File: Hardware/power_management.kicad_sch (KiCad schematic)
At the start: 34 parts, among them J2 Conn_01x03, SW27 SW_DPDT_x2, U2 BQ24040, U3 BQ51050BRHL, U4 AP22814BW5

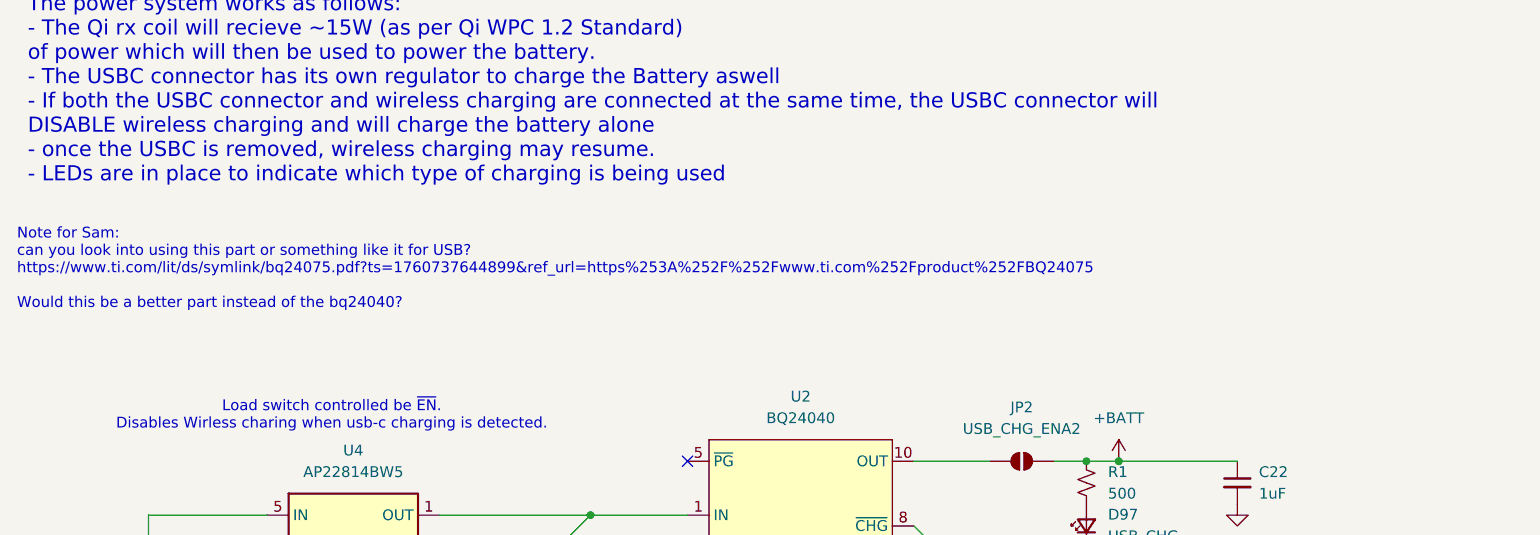
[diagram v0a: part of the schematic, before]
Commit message: Route dual sided hotswap/diodes assmebly
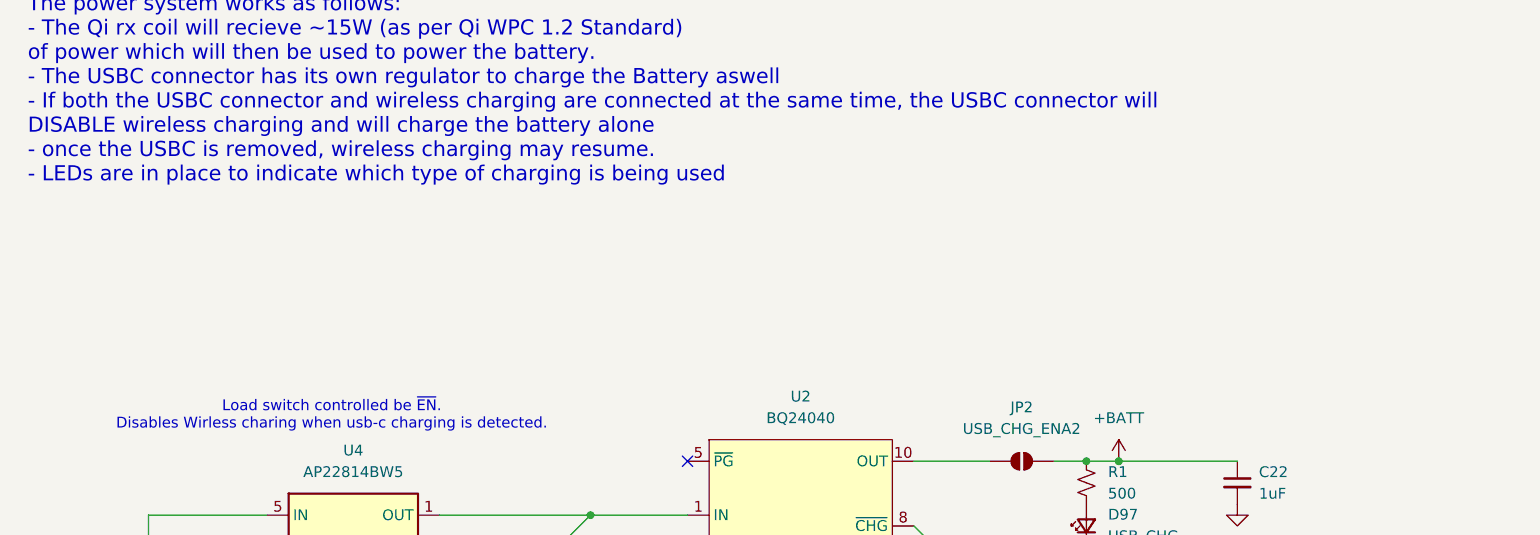
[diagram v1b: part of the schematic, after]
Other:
- note removed: "Note for Sam: can you look into using this part or something like it for USB? https://www.ti.com/lit/ds/symlink/bq24075.pdf?ts=1760737644899&ref_url=https%253A%252F%252Fwww.ti.com%252Fproduct%252FBQ24075 Would this be a better part instead of the bq24040?"
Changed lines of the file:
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@@
-		)
-	)
-	(text "Note for Sam:\ncan you look into using this part or something like it for USB?\nhttps://www.ti.com/lit/ds/symlink/bq24075.pdf?ts=1760737644899&ref_url=https%253A%252F%252Fwww.ti.com%252Fproduct%252FBQ24075\n\nWould this be a better part instead of the bq24040? "
-		(exclude_from_sim no)
-		(at 13.716 47.244 0)
-		(effects
-			(font
-				(size 1.27 1.27)
-			)
-			(justify left)
 		)
 	)

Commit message: added extra decoupling caps to the mcu VDD pins
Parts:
- J2: footprint Connector_JST:JST_GH_SM02B-GHS-TB_1x02-1MP_P1.25mm_Horizontal -> Connector_JST:JST_GH_SM03B-GHS-TB_1x03-1MP_P1.25mm_Horizontal
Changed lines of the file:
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@@
 			)
 		)
-		(property "Footprint" "Connector_JST:JST_GH_SM02B-GHS-TB_1x02-1MP_P1.25mm_Horizontal"
+		(property "Footprint" "Connector_JST:JST_GH_SM03B-GHS-TB_1x03-1MP_P1.25mm_Horizontal"
 			(at 190.5 128.27 0)
 			(effects

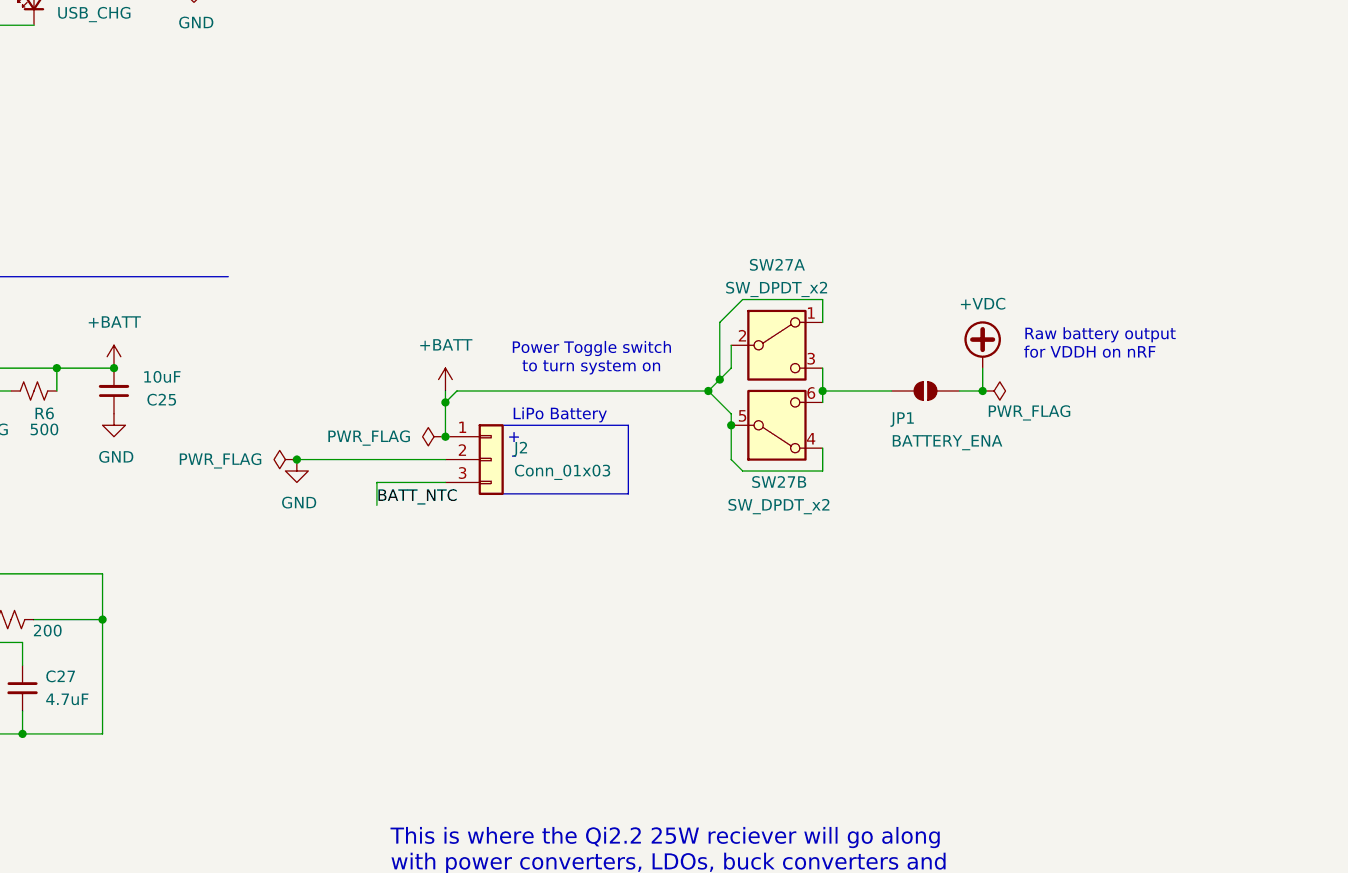
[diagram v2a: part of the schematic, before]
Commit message: added in pwoer mux
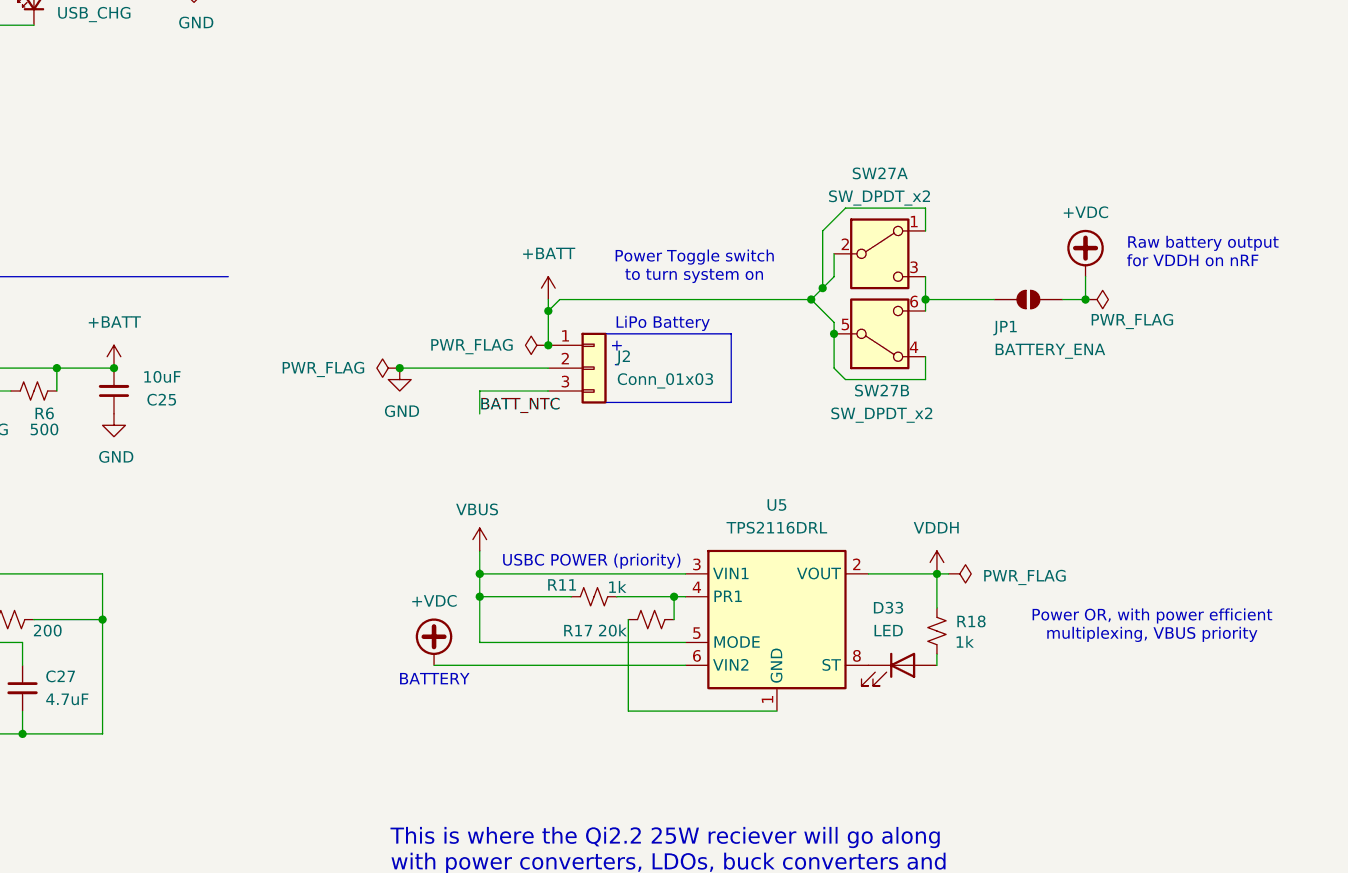
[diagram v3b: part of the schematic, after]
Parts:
- added D33: LED, symbol Device:LED
- added R11, R18: 1k, Resistor_SMD:R_0603_1608Metric, symbol Device:R_Small_US
- added R17: 20k, Resistor_SMD:R_0603_1608Metric, symbol Device:R_Small_US
- added U5: TPS2116DRL, Package_TO_SOT_SMD:SOT-583-8, symbol Power_Management:TPS2116DRL
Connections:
- net +VDC: now also U5.6 (VIN2)
- net VBUS: now also R11.1, U5.3 (VIN1), U5.5 (MODE)
- new net: R11.2, R17.1, U5.4 (PR1)
- new net: R17.2, U5.1 (GND)
- new net: D33.1 (K), U5.8 (ST)
- new net: D33.2 (A), R18.1
- new net VDDH: R18.2, U5.2 (VOUT), U5.7 (VOUT)
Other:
- note added: "BATTERY"
- note added: "Power OR, with power efficient multiplexing, VBUS priority"
- note added: "USBC POWER (priority)"
- moved on the sheet: J2, JP1, SW27A, SW27B

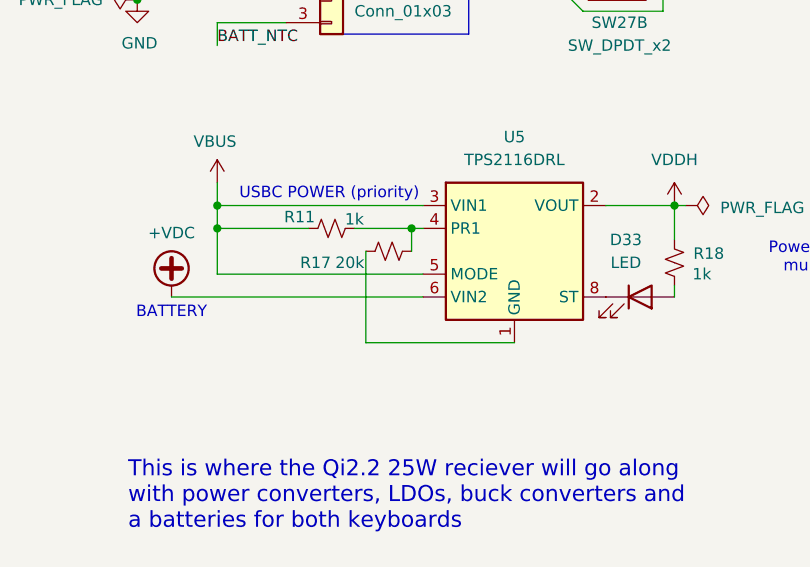
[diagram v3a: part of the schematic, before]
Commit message: modified layout placement
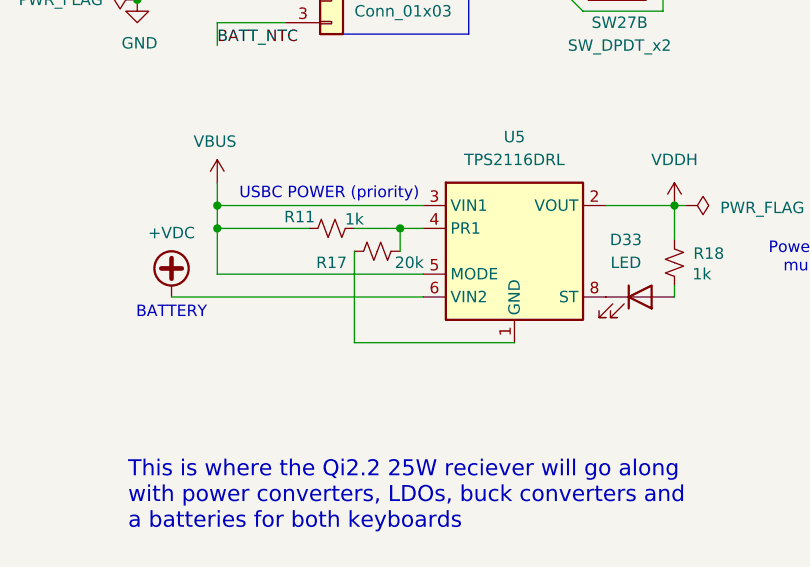
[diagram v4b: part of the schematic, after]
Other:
- moved on the sheet: R17
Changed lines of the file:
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@@
 	)
 	(junction
+		(at 209.55 143.51)
+		(diameter 0)
+		(color 0 0 0 0)
+	)
+	(junction
 		(at 227.33 109.22)
 		(diameter 0)
@@
 	)
 	(junction
-		(at 210.82 143.51)
-		(diameter 0)
-		(color 0 0 0 0)
-	)
-	(junction
 		(at 130.81 146.05)
 		(diameter 0)
@@
 		)
 	)
+	(wire
+		(pts
+			(xy 209.55 143.51) (xy 212.09 143.51)
+		)
+		(stroke
+			(width 0)
+			(type default)
+		)
+	)
 	(polyline
 		(pts
@@
 	(wire
 		(pts
-			(xy 205.74 146.05) (xy 205.74 156.21)
+			(xy 204.47 146.05) (xy 204.47 156.21)
 		)
 		(stroke
@@
 	(wire
 		(pts
-			(xy 210.82 143.51) (xy 212.09 143.51)
-		)
-		(stroke
-			(width 0)
-			(type default)
-		)
-	)
-	(wire
-		(pts
 			(xy 227.33 109.22) (xy 226.06 110.49)
 		)
@@
 	(wire
 		(pts
-			(xy 210.82 143.51) (xy 210.82 146.05)
+			(xy 209.55 143.51) (xy 209.55 146.05)
 		)
 		(stroke
@@
 	(wire
 		(pts
-			(xy 205.74 156.21) (xy 222.25 156.21)
+			(xy 204.47 156.21) (xy 222.25 156.21)
 		)
 		(stroke
@@
 	(wire
 		(pts
-			(xy 204.47 143.51) (xy 210.82 143.51)
+			(xy 204.47 143.51) (xy 209.55 143.51)
 		)
 		(stroke
@@
 	(symbol
 		(lib_id "Device:R_Small_US")
-		(at 208.28 146.05 270)
+		(at 207.01 146.05 270)
 		(unit 1)
 		(exclude_from_sim no)
@@
 		(dnp no)
 		(property "Reference" "R17"
-			(at 200.152 147.32 90)
+			(at 201.93 147.32 90)
 			(effects
 				(font
@@
 		)
 		(property "Value" "20k"
-			(at 203.962 147.32 90)
+			(at 210.566 147.32 90)
 			(effects
 				(font
@@
 		)
 		(property "Footprint" "Resistor_SMD:R_0603_1608Metric"
-			(at 208.28 146.05 0)
+			(at 207.01 146.05 0)
 			(effects
 				(font
@@
 		)
 		(property "Datasheet" "~"
-			(at 208.28 146.05 0)
+			(at 207.01 146.05 0)
 			(effects
 				(font
@@
 		)
 		(property "Description" "Resistor, small US symbol"
-			(at 208.28 146.05 0)
+			(at 207.01 146.05 0)
 			(effects
 				(font

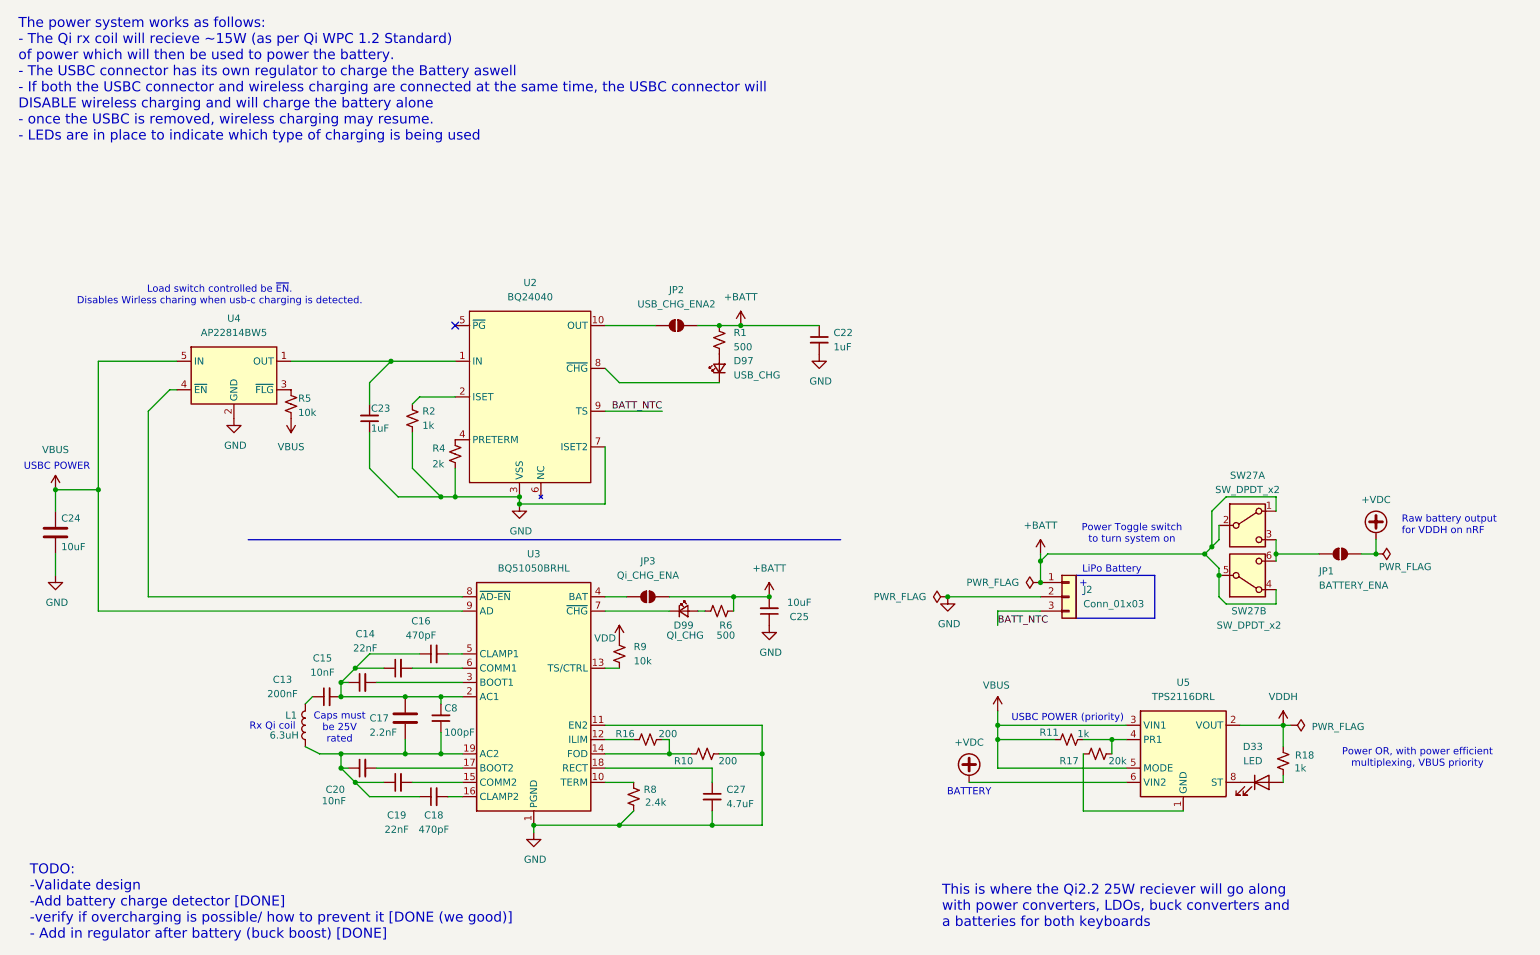
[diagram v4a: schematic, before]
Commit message: Fix ERC and stylistic errors
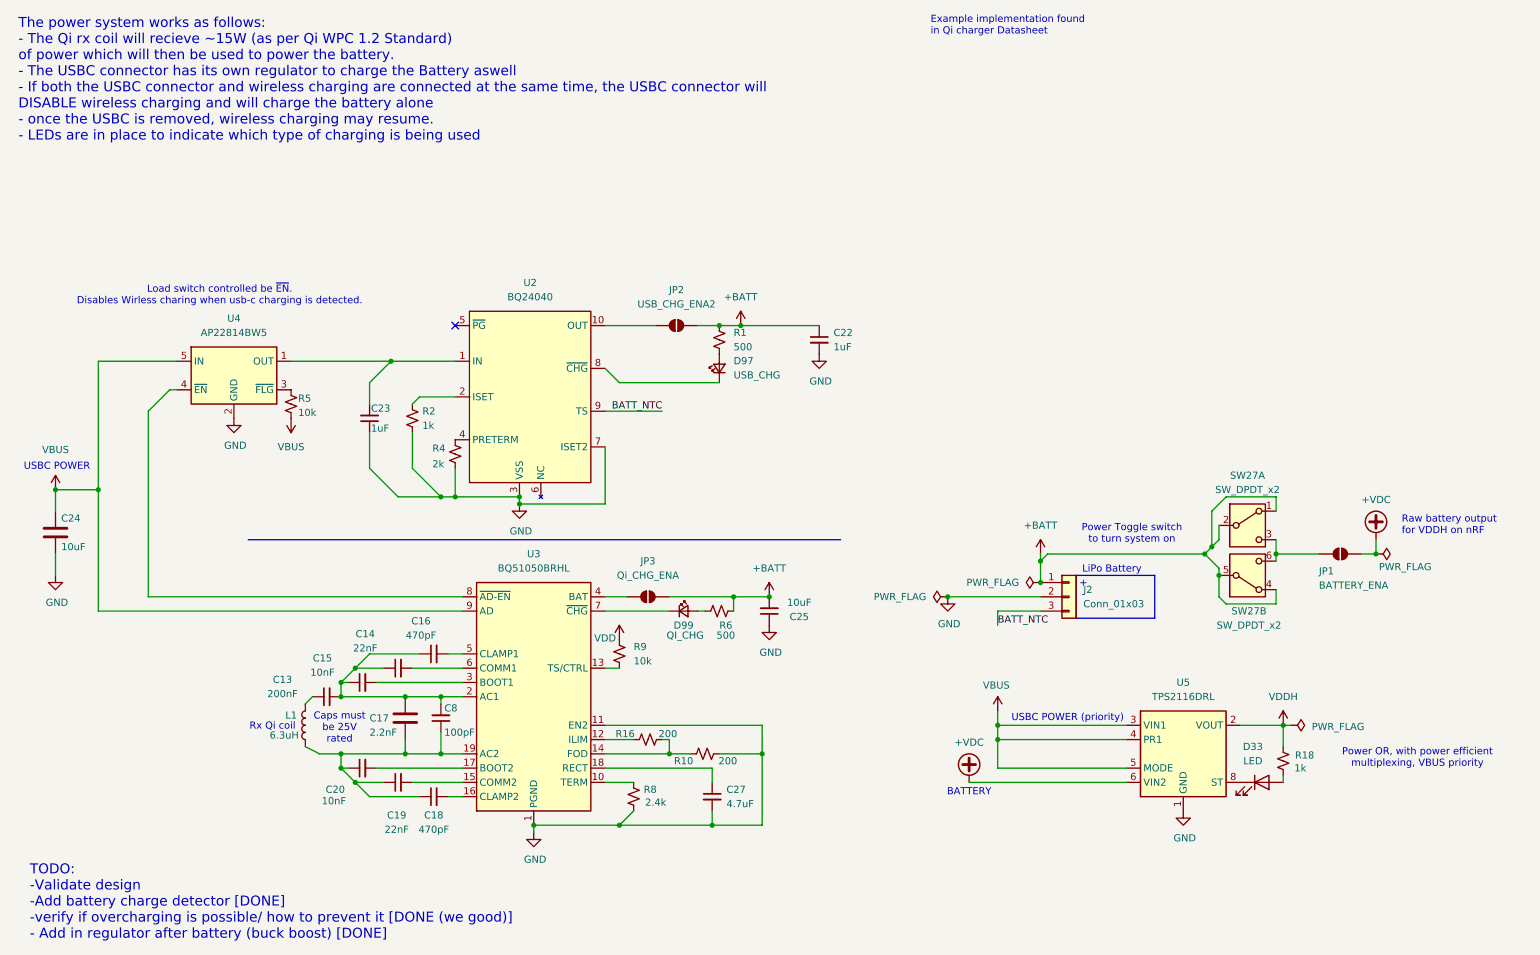
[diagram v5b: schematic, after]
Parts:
- removed R11: 1k, Resistor_SMD:R_0603_1608Metric, symbol Device:R_Small_US
- removed R17: 20k, Resistor_SMD:R_0603_1608Metric, symbol Device:R_Small_US
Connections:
- net GND: now also U5.1 (GND)
- net VBUS: now also U5.4 (PR1)
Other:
- note added: "Example implementation found in Qi charger Datasheet"
- note removed: "This is where the Qi2.2 25W reciever will go along with power converters, LDOs, buck converters and a batteries for both keyboards"

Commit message: Add Antenna Library to repo
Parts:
- D33: footprint (none) -> LED_SMD:LED_0805_2012Metric
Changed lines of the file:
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@@
 			)
 		)
-		(property "Footprint" ""
+		(property "Footprint" "LED_SMD:LED_0805_2012Metric"
 			(at 236.22 151.13 0)
 			(effects

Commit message: Completed mcu routing
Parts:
- D33: footprint LED_SMD:LED_0805_2012Metric -> LED_SMD:LED_0402_1005Metric
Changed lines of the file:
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@@
 			)
 		)
-		(property "Footprint" "LED_SMD:LED_0805_2012Metric"
+		(property "Footprint" "LED_SMD:LED_0402_1005Metric"
 			(at 236.22 151.13 0)
 			(effects
